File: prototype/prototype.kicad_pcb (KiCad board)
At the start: 4 copper layers, 78.7 x 63.5 mm, 47 parts, among them P1 CONN_25X2, P2 CONN_25X2, P3 VGACONN, U1 MC68SEC000, U2 FLASHROM_512K_16, U3 RAM_512K_16, U4 RAM_512K_16

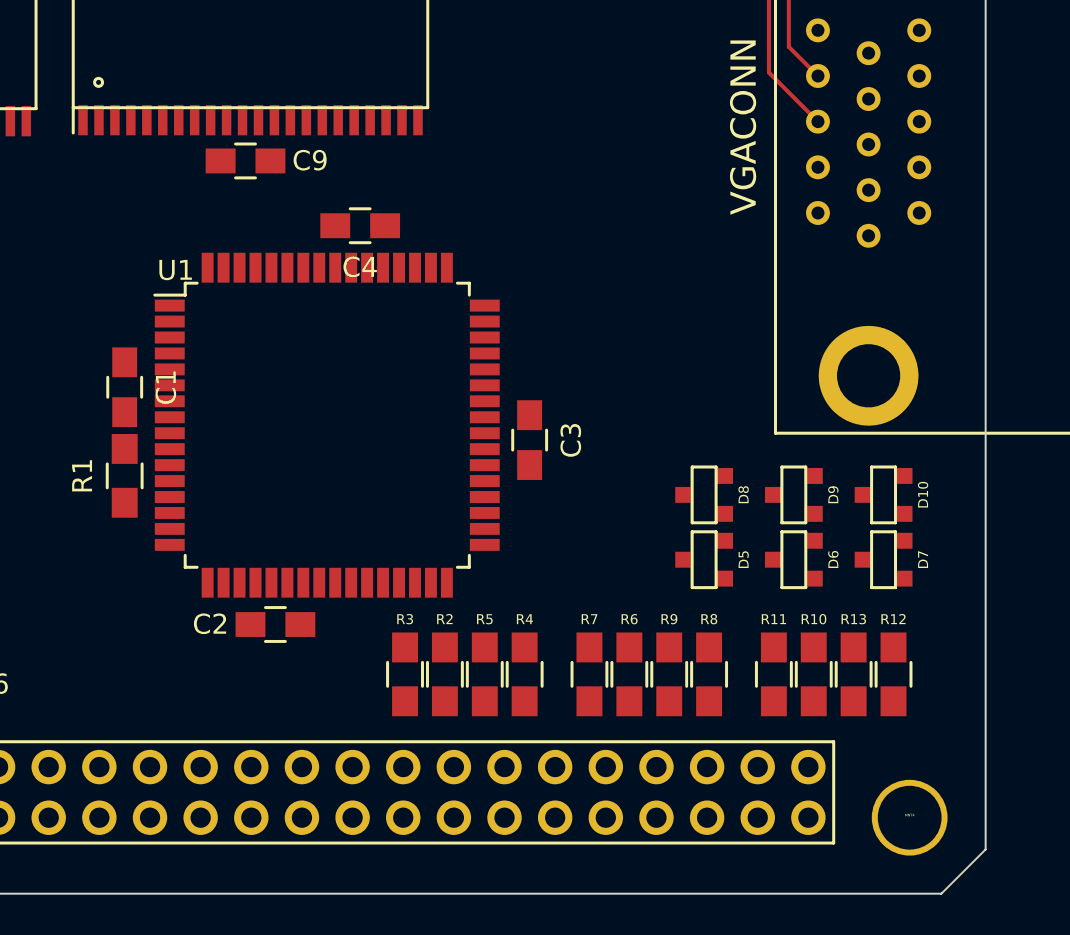
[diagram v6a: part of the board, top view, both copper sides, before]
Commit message: Route RGB signals and 68k decoupling caps.
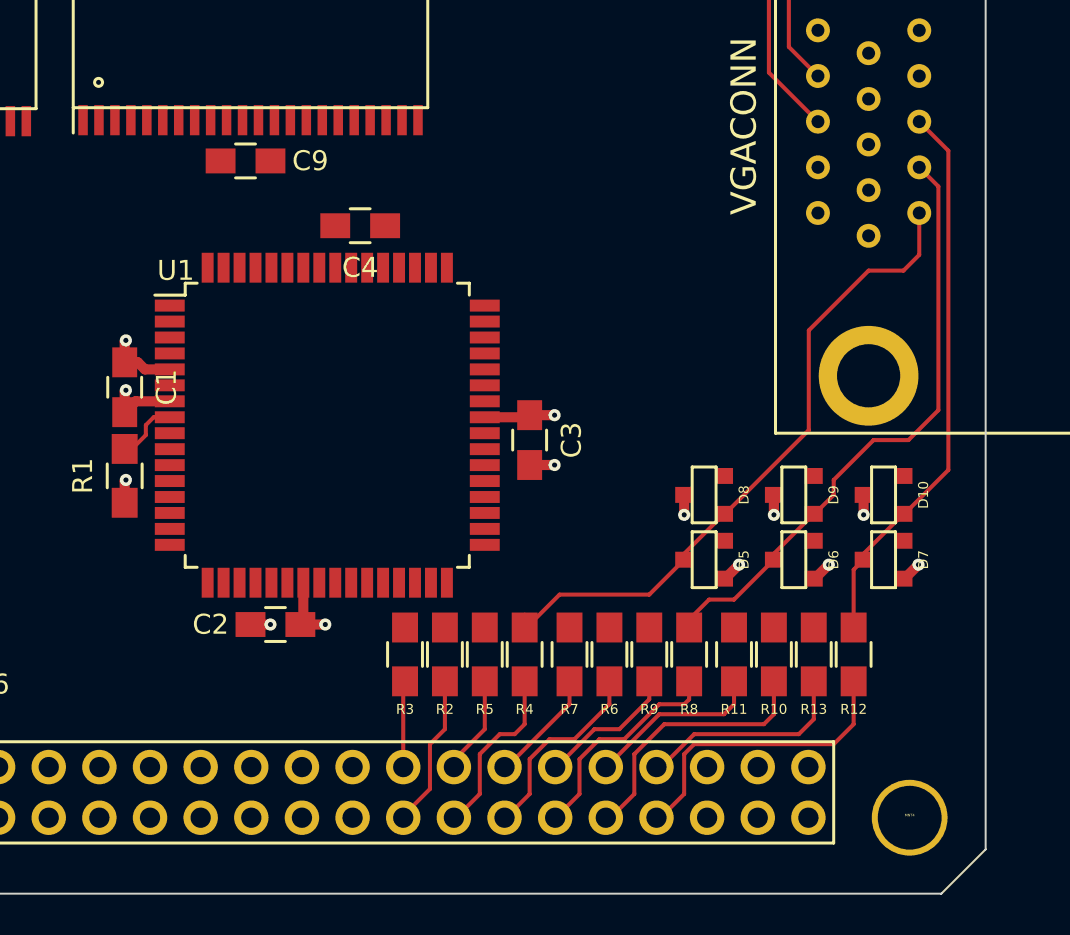
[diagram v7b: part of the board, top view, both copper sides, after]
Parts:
- moved R10 2.24 mm to (180.5, 112.5)
- moved R11 2.24 mm to (178.5, 112.5)
- moved R12 2.24 mm to (184.5, 112.5)
- moved R13 2.24 mm to (182.5, 112.5)
- moved R6 1.41 mm to (172.3, 112.5)
- moved R7 1.41 mm to (170.3, 112.5)
- moved R8 1.41 mm to (176.3, 112.5)
- moved R9 1.41 mm to (174.3, 112.5)
- moved R2 1.00 mm to (164.0, 112.5)
- moved R3 1.00 mm to (162.0, 112.5)
- moved R4 1.00 mm to (168.0, 112.5)
- moved R5 1.00 mm to (166.0, 112.5)
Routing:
- net RED: track 0.00 -> 33.4 mm
- net GREEN: track 0.00 -> 30.8 mm
- net BLUE: track 0.00 -> 28.3 mm
- net BLUE2: track 0.00 -> 15.6 mm
- net BLUE0: track 0.00 -> 13.9 mm
- net VCC: track 0.00 -> 12.2 mm, vias 0 -> 7
- net GND: track 2.31 -> 13.7 mm, vias 2 -> 8
- net GREEN2: track 0.00 -> 11.1 mm
- net BLUE3: track 0.00 -> 10.8 mm
- net GREEN0: track 0.00 -> 9.79 mm
- net BLUE1: track 0.00 -> 8.88 mm
- net RED2: track 0.00 -> 8.81 mm
- net RED0: track 0.00 -> 7.71 mm
- net GREEN3: track 0.00 -> 7.03 mm
- net GREEN1: track 0.00 -> 5.71 mm
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
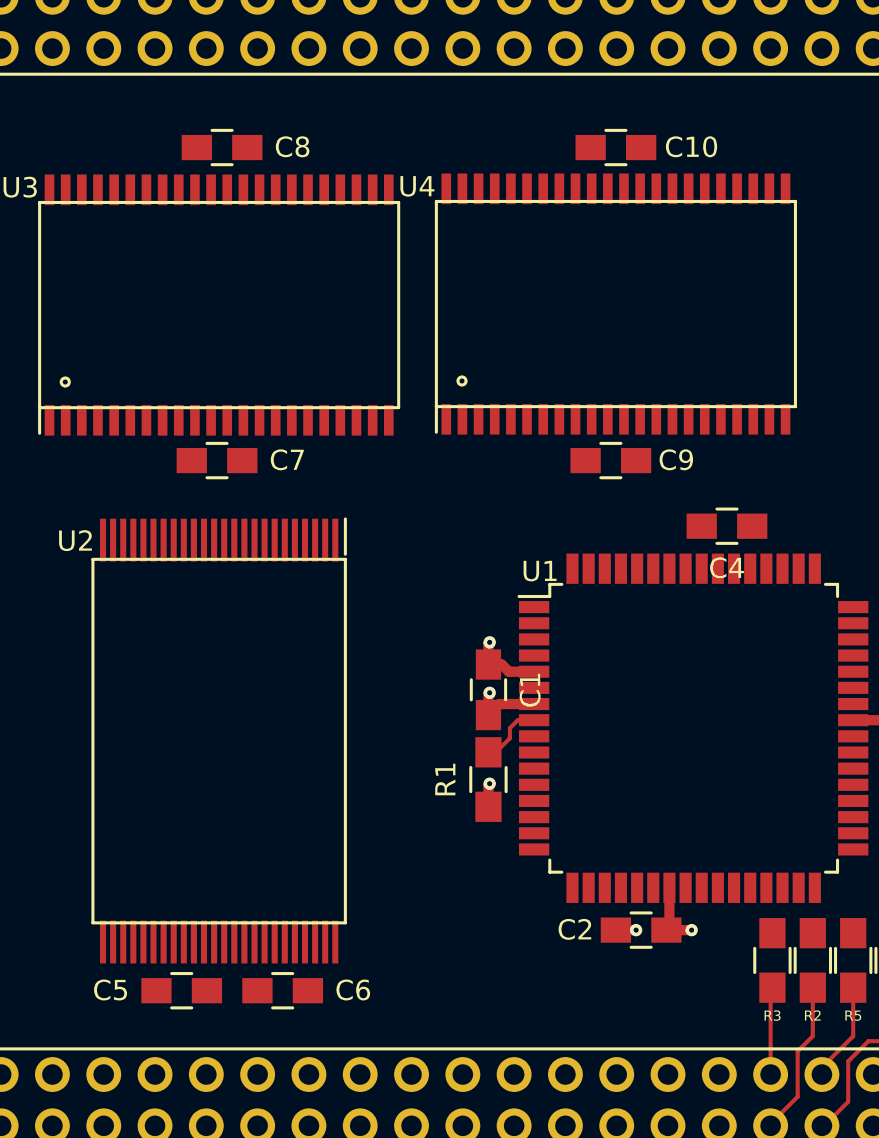
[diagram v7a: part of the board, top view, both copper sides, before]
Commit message: Route the remaining IC power supplies and decoupling caps.
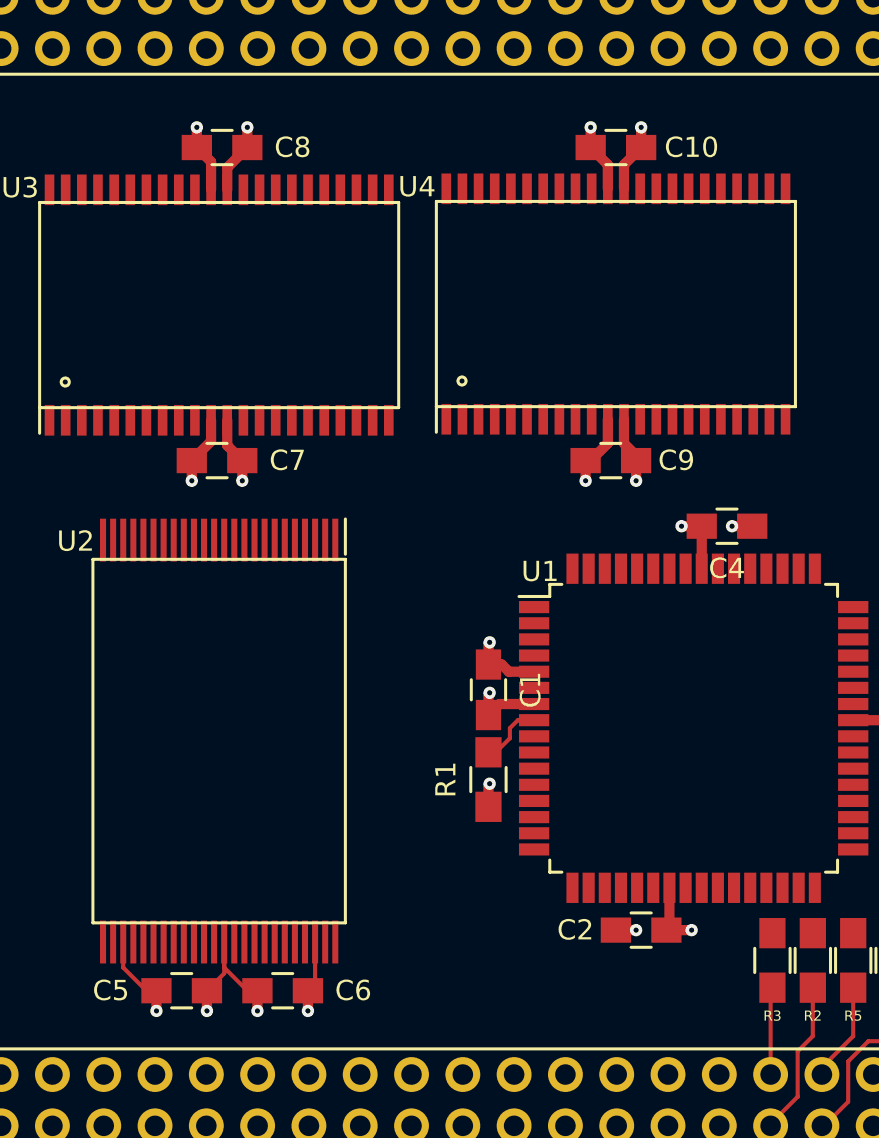
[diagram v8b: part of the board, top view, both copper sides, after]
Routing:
- net GND: track 13.7 -> 38.1 mm, vias 8 -> 15
- net VCC: track 12.2 -> 35.3 mm, vias 7 -> 14
